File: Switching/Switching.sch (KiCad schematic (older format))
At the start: 11 parts

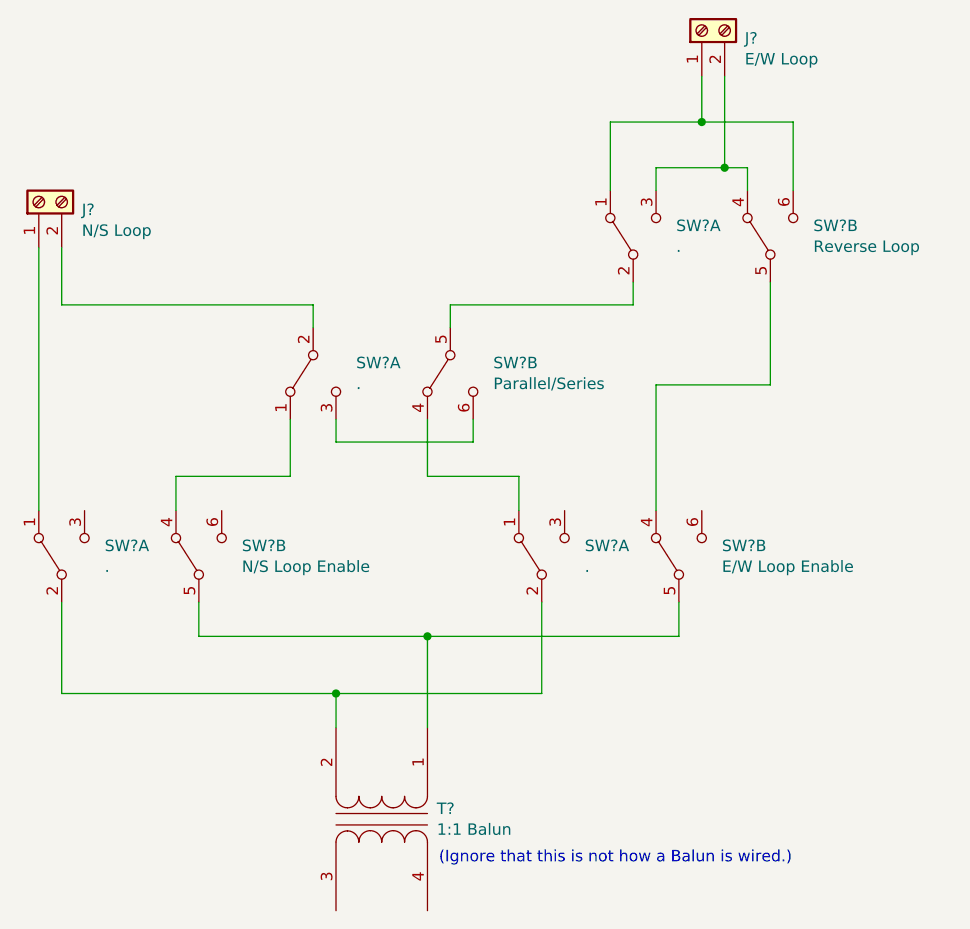
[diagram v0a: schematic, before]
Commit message: First draft of BayCon 2021 presentation.
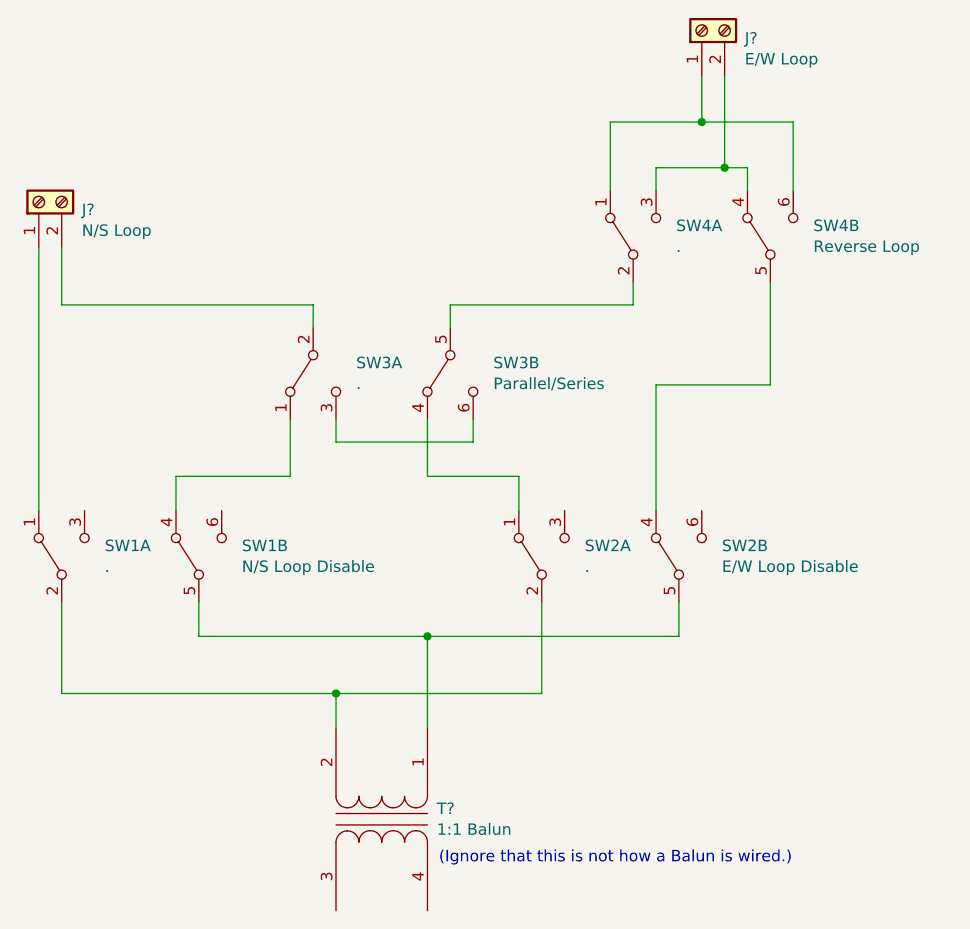
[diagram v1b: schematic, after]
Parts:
- SW1: renamed from SW?; value N/S Loop Enable -> N/S Loop Disable
- SW2: renamed from SW?; value E/W Loop Enable -> E/W Loop Disable
- gave numbers to parts that had none: 4
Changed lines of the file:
@@
 EESchema Schematic File Version 4
+LIBS:Switching-cache
 EELAYER 26 0
 EELAYER END
@@
 $EndDescr
 $Comp
-L Switch:SW_DPDT_x2 SW?
+L Switch:SW_DPDT_x2 SW1
 U 1 1 5F683237
 P 3700 4100
-F 0 "SW?" V 3746 3912 50  0000 R CNN
+F 0 "SW1" V 3746 3912 50  0000 R CNN
 F 1 "." V 3655 3912 50  0000 R CNN
 F 2 "" H 3700 4100 50  0001 C CNN
@@
 $EndComp
 $Comp
-L Switch:SW_DPDT_x2 SW?
+L Switch:SW_DPDT_x2 SW1
 U 2 1 5F6832B9
 P 4300 4100
-F 0 "SW?" V 4346 3912 50  0000 R CNN
-F 1 "N/S Loop Enable" V 4255 3912 50  0000 R CNN
+F 0 "SW1" V 4346 3912 50  0000 R CNN
+F 1 "N/S Loop Disable" V 4255 3912 50  0000 R CNN
 F 2 "" H 4300 4100 50  0001 C CNN
 F 3 "" H 4300 4100 50  0001 C CNN
@@
 $EndComp
 $Comp
-L Switch:SW_DPDT_x2 SW?
+L Switch:SW_DPDT_x2 SW2
 U 1 1 5F68339C
 P 5800 4100
-F 0 "SW?" V 5846 3912 50  0000 R CNN
+F 0 "SW2" V 5846 3912 50  0000 R CNN
 F 1 "." V 5755 3912 50  0000 R CNN
 F 2 "" H 5800 4100 50  0001 C CNN
@@
 $EndComp
 $Comp
-L Switch:SW_DPDT_x2 SW?
+L Switch:SW_DPDT_x2 SW2
 U 2 1 5F6833A3
 P 6400 4100
-F 0 "SW?" V 6446 3912 50  0000 R CNN
-F 1 "E/W Loop Enable" V 6355 3912 50  0000 R CNN
+F 0 "SW2" V 6446 3912 50  0000 R CNN
+F 1 "E/W Loop Disable" V 6355 3912 50  0000 R CNN
 F 2 "" H 6400 4100 50  0001 C CNN
 F 3 "" H 6400 4100 50  0001 C CNN
@@
 $EndComp
 $Comp
-L Switch:SW_DPDT_x2 SW?
+L Switch:SW_DPDT_x2 SW3
 U 1 1 5F683663
 P 4800 3300
-F 0 "SW?" V 4754 3112 50  0000 R CNN
+F 0 "SW3" V 4754 3112 50  0000 R CNN
 F 1 "." V 4845 3112 50  0000 R CNN
 F 2 "" H 4800 3300 50  0001 C CNN
@@
 $EndComp
 $Comp
-L Switch:SW_DPDT_x2 SW?
+L Switch:SW_DPDT_x2 SW3
 U 2 1 5F68366A
 P 5400 3300
-F 0 "SW?" V 5354 3112 50  0000 R CNN
+F 0 "SW3" V 5354 3112 50  0000 R CNN
 F 1 "Parallel/Series" V 5445 3112 50  0000 R CNN
 F 2 "" H 5400 3300 50  0001 C CNN
@@
 $EndComp
 $Comp
-L Switch:SW_DPDT_x2 SW?
+L Switch:SW_DPDT_x2 SW4
 U 1 1 5F68378F
 P 6200 2700
-F 0 "SW?" V 6246 2512 50  0000 R CNN
+F 0 "SW4" V 6246 2512 50  0000 R CNN
 F 1 "." V 6155 2512 50  0000 R CNN
 F 2 "" H 6200 2700 50  0001 C CNN
@@
 $EndComp
 $Comp
-L Switch:SW_DPDT_x2 SW?
+L Switch:SW_DPDT_x2 SW4
 U 2 1 5F683796
 P 6800 2700
-F 0 "SW?" V 6846 2512 50  0000 R CNN
+F 0 "SW4" V 6846 2512 50  0000 R CNN
 F 1 "Reverse Loop" V 6755 2512 50  0000 R CNN
 F 2 "" H 6800 2700 50  0001 C CNN
